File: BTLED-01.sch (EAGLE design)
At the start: 17 parts

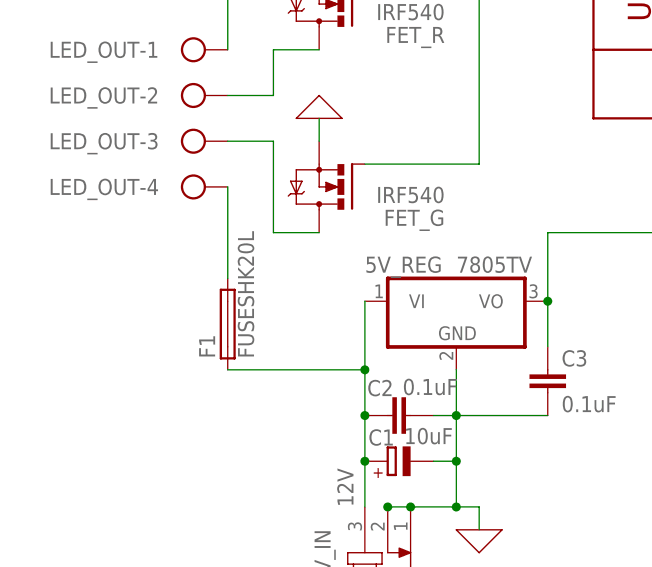
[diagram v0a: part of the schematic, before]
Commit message: fix: Replace fuse holder footprint
Replace 20mm fuse footprint with 22.5mm fuse holder.
Tweak some trace widths
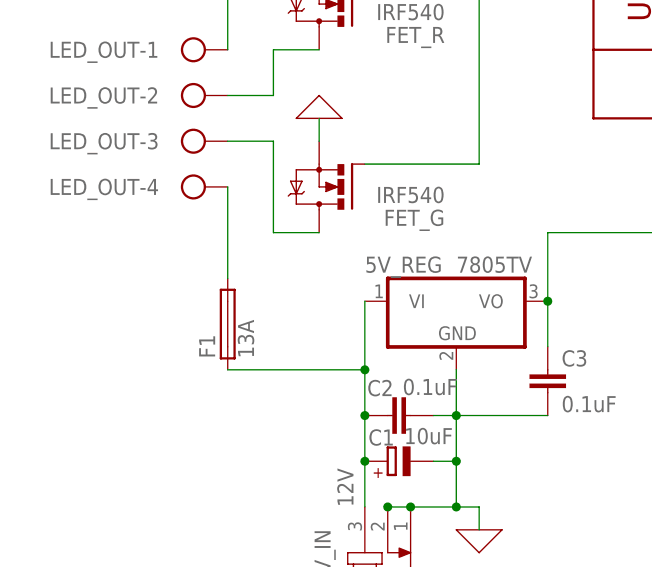
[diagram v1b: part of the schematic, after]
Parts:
- F1: value FUSESHK20L -> 13A; device fuse:FUSESHK20L -> fuse:SH22,5
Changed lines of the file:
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@@
 </variantdefs>
 <classes>
-<class number="0" name="default" width="0.4064" drill="0.6096">
+<class number="0" name="default" width="0.3048" drill="0.6096">
 <clearance class="0" value="0.254"/>
 </class>
@@
 <part name="5V_REG" library="linear" library_urn="urn:adsk.eagle:library:262" deviceset="78*" device="TV" package3d_urn="urn:adsk.eagle:package:16417/2" technology="05"/>
 <part name="X_5" library="ngspice-simulation" library_urn="urn:adsk.eagle:library:527439" deviceset="GND" device=""/>
-<part name="F1" library="fuse" library_urn="urn:adsk.eagle:library:233" deviceset="FUSE" device="SHK20L" package3d_urn="urn:adsk.eagle:package:14071/1"/>
+<part name="F1" library="fuse" library_urn="urn:adsk.eagle:library:233" deviceset="SH22,5" device="" package3d_urn="urn:adsk.eagle:package:14059/1" value="13A"/>
 <part name="C1" library="rcl" library_urn="urn:adsk.eagle:library:334" deviceset="CPOL-EU" device="E2.5-6" package3d_urn="urn:adsk.eagle:package:23349/1" value="10uF"/>
 <part name="C2" library="rcl" library_urn="urn:adsk.eagle:library:334" deviceset="C-EU" device="050-024X044" package3d_urn="urn:adsk.eagle:package:23643/1" value="0.1uF"/>
@@
 </instance>
 <instance part="X_5" gate="G$1" x="93.98" y="12.7" smashed="yes"/>
-<instance part="F1" gate="G$1" x="-5.08" y="2.54" smashed="yes" rot="R90">
+<instance part="F1" gate="1" x="-5.08" y="2.54" smashed="yes" rot="R90">
 <attribute name="NAME" x="-6.477" y="-1.27" size="1.778" layer="95" rot="R90"/>
 <attribute name="VALUE" x="-2.159" y="-1.27" size="1.778" layer="96" rot="R90"/>
@@
 <segment>
 <pinref part="LED_OUT" gate="-4" pin="KL"/>
-<pinref part="F1" gate="G$1" pin="2"/>
+<pinref part="F1" gate="1" pin="2"/>
 <wire x1="-5.08" y1="17.78" x2="-5.08" y2="7.62" width="0.1524" layer="91"/>
 </segment>
@@
 <net name="12V_IN" class="0">
 <segment>
-<pinref part="F1" gate="G$1" pin="1"/>
+<pinref part="F1" gate="1" pin="1"/>
 <pinref part="12V_IN" gate="G$1" pin="3"/>
 <wire x1="-5.08" y1="-2.54" x2="10.16" y2="-2.54" width="0.1524" layer="91"/>

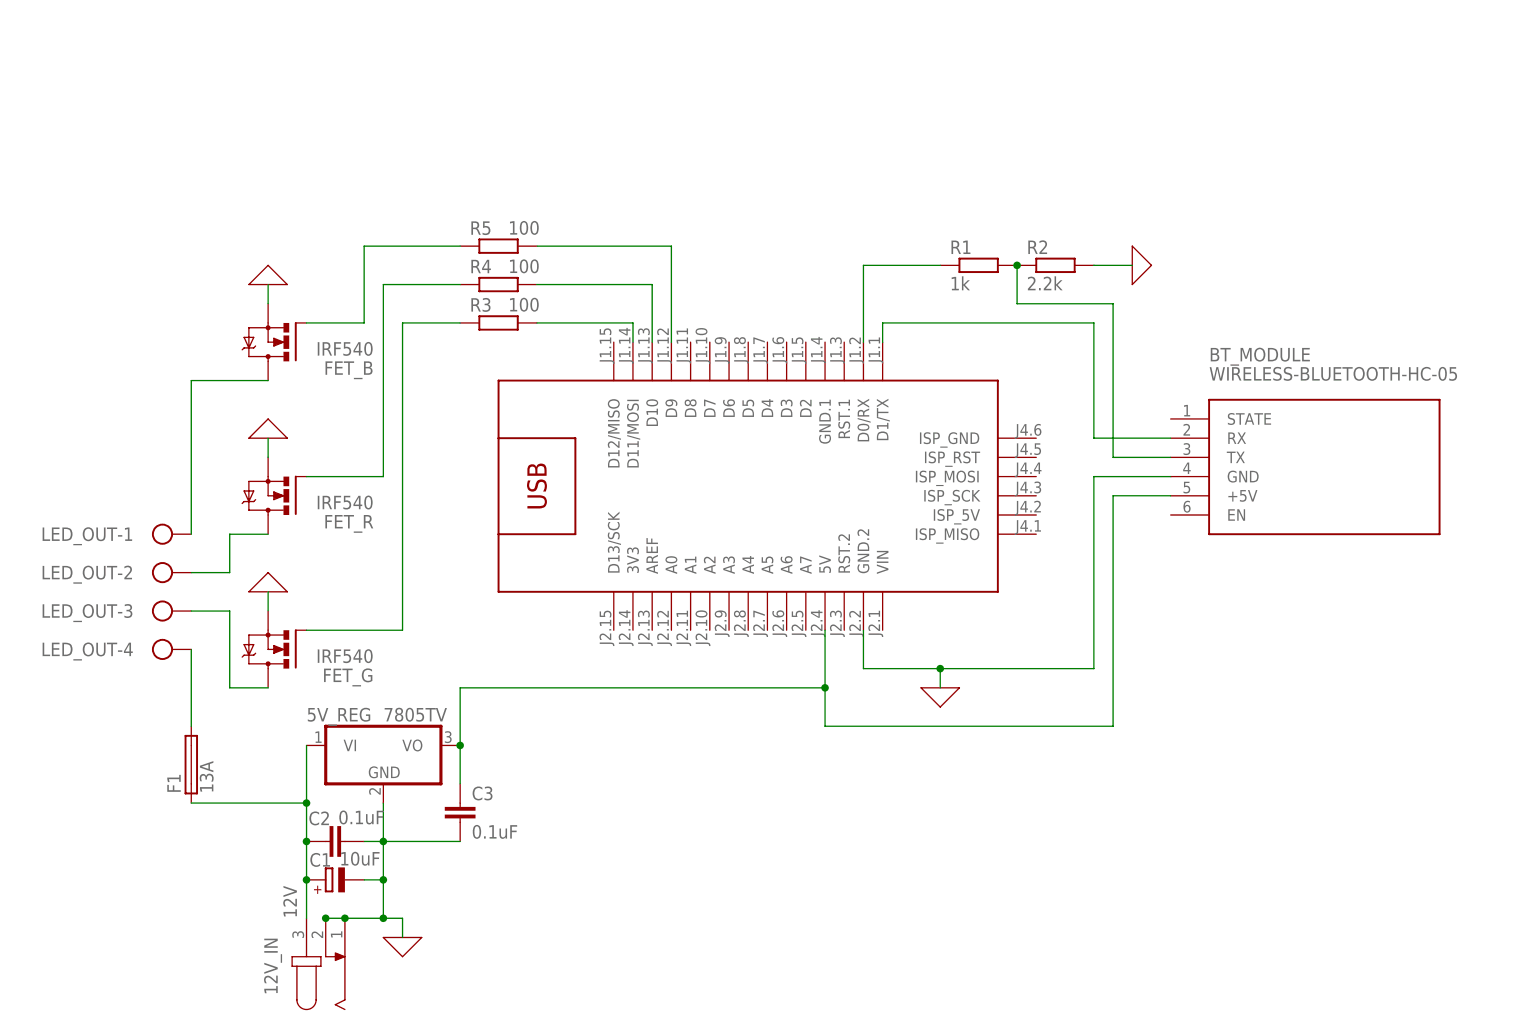
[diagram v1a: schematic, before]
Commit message: feat: Add pulldown resistors to MOSFET gate signals
BREAKING CHANGE: Switched TX/RX pins on Arduino to avoid conflicts with
built-in serial
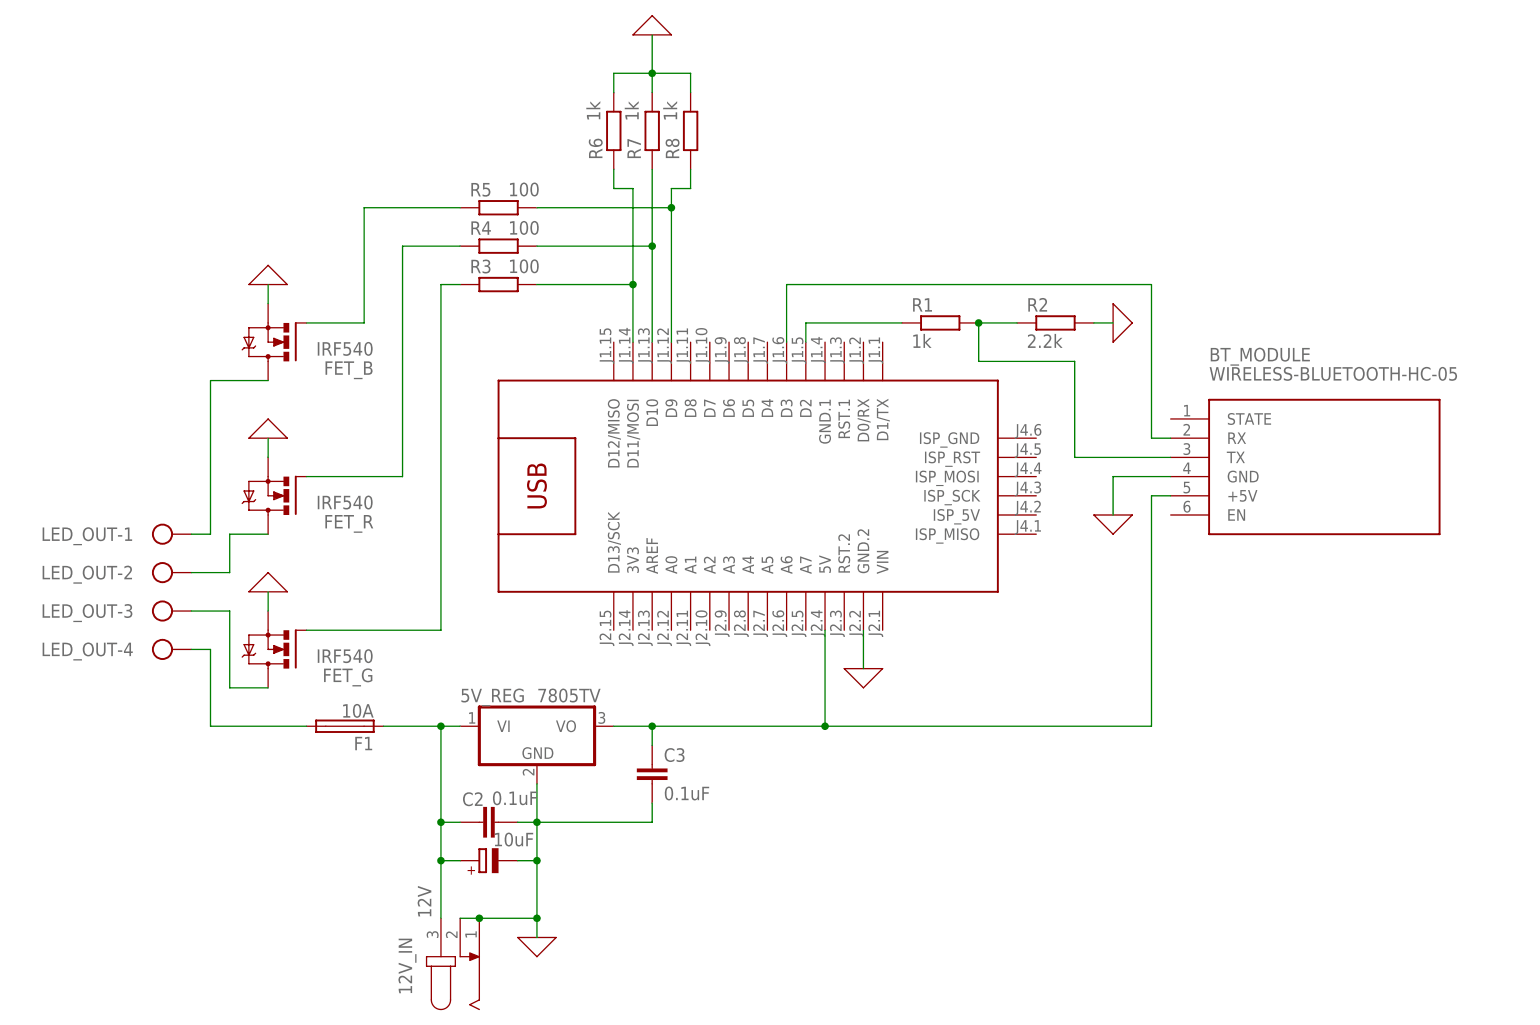
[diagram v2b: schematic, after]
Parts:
- added R6, R7, R8: 1k, rcl:R-EU_0204/7
- F1: value 13A -> 10A
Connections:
- net BT_TX_3.3V renamed BT_RX_3.3V
- removed net BT_RX: ARDUINO_NANO.D1/TX, BT_MODULE.RX
- removed net BT_TX_5V: ARDUINO_NANO.D0/RX, R1.1
- new net BT_RX_5V: ARDUINO_NANO.D2, R1.1
- new net BT_TX: ARDUINO_NANO.D3, BT_MODULE.RX
- net B_SIG_1: now also R8.1
- net GND: now also R6.2, R7.2, R8.2
- net G_SIG_1: now also R6.1
- net R_SIG_1: now also R7.1
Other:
- moved on the sheet: 12V_IN, 5V_REG, C2, C3, F1, R1, R2, R3, R4, R5
